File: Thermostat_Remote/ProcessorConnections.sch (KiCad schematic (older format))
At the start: 4 parts

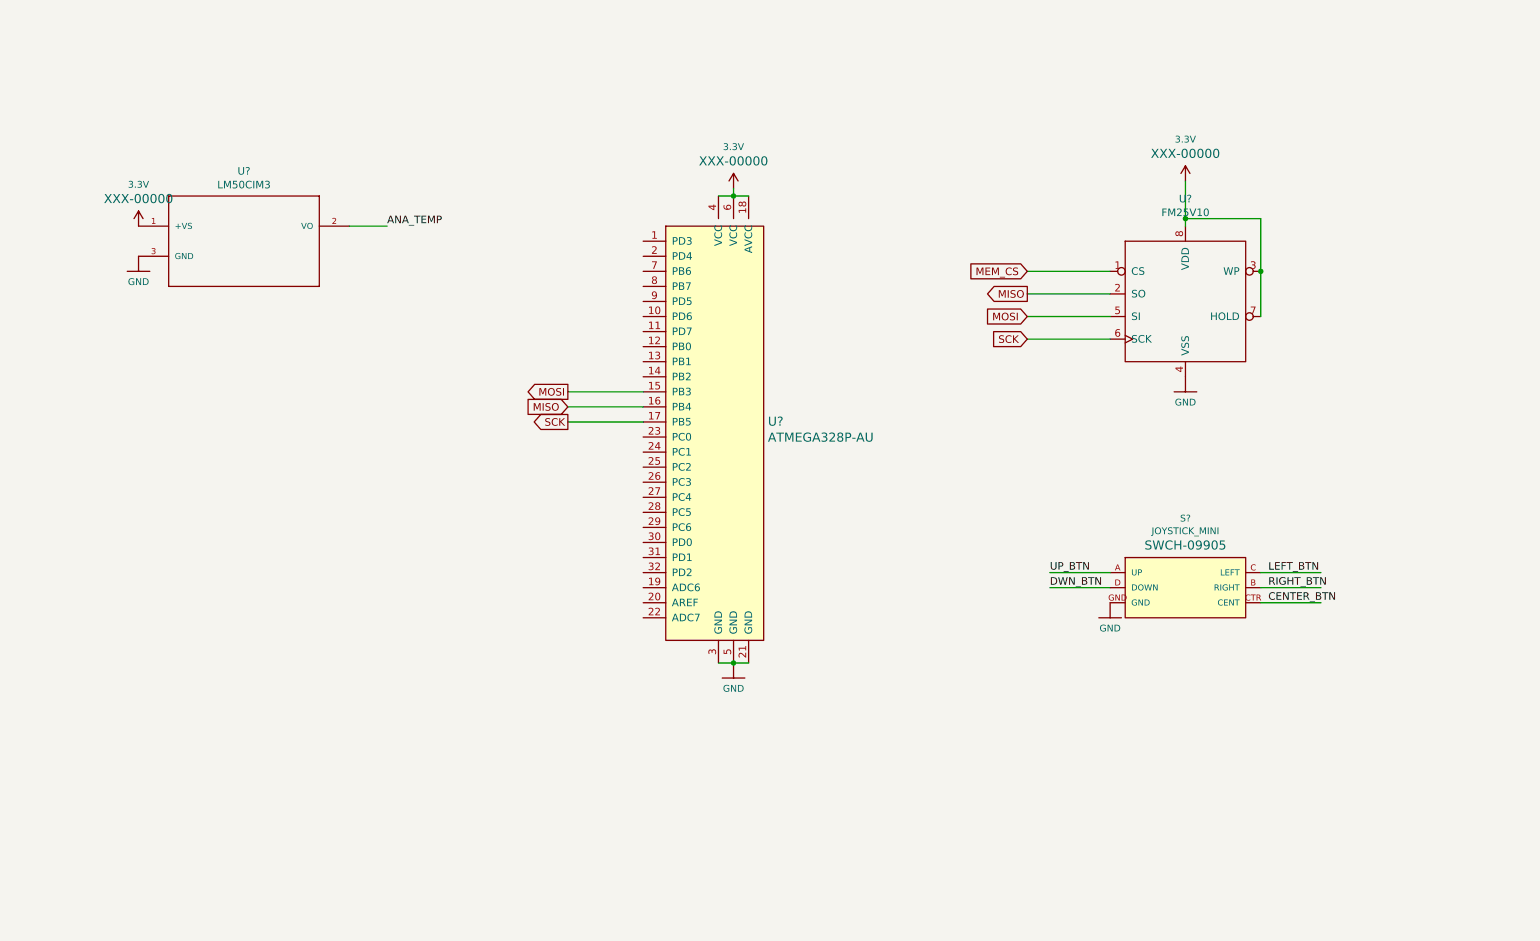
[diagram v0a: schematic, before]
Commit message: Update remote sensor layout
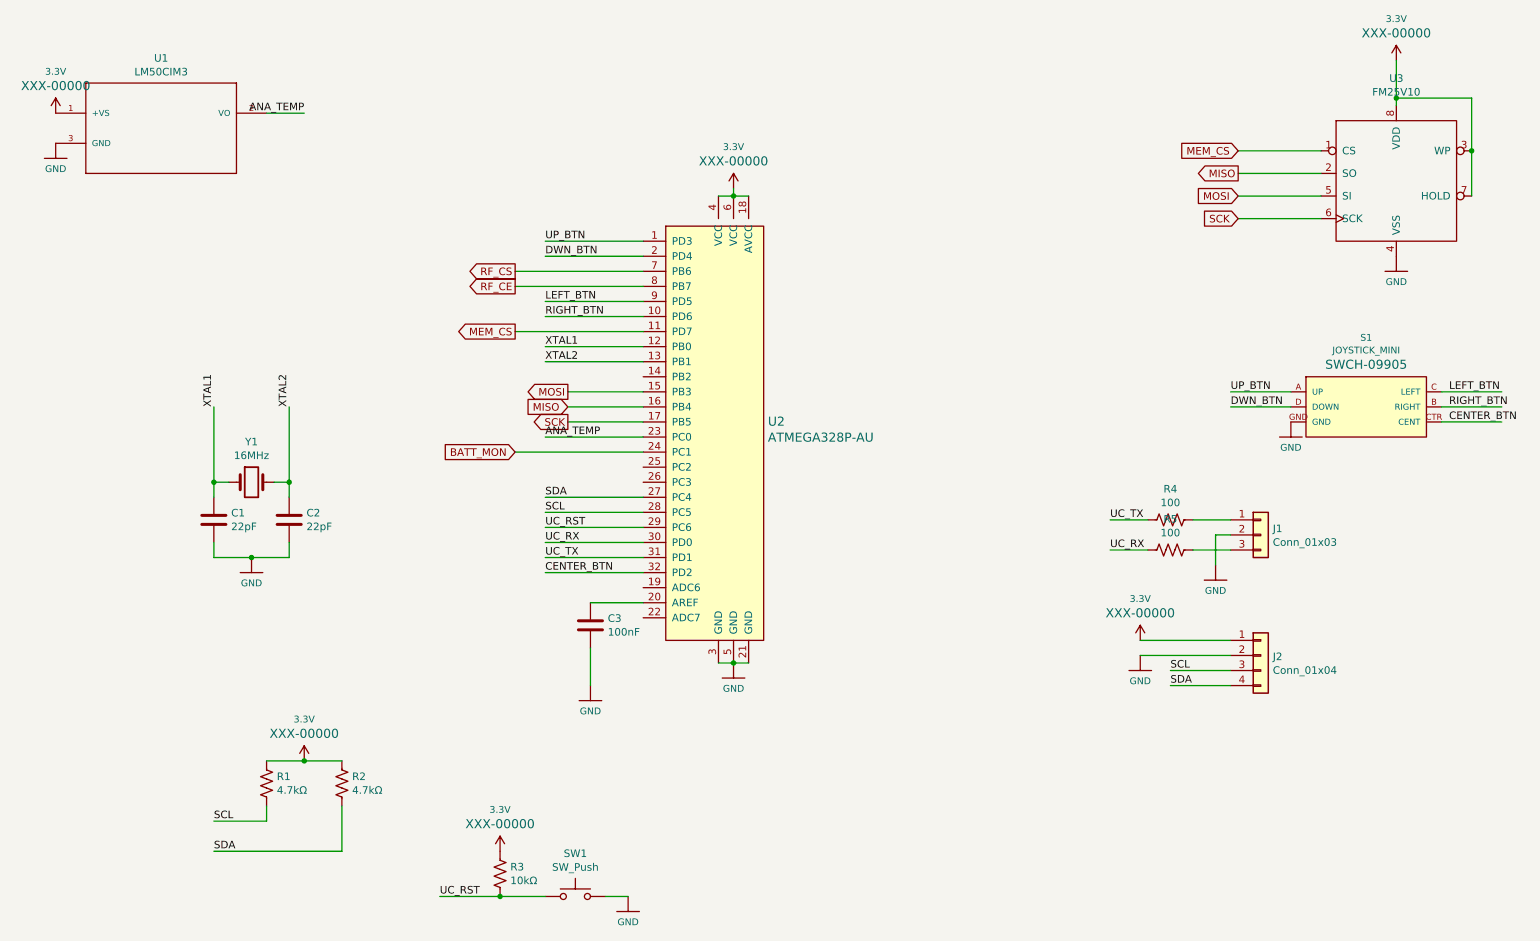
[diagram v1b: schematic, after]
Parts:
- added C1, C2: 22pF, Capacitor_SMD:C_0402_1005Metric, symbol Device:C
- added C3: 100nF, Capacitor_SMD:C_0402_1005Metric, symbol Device:C
- added J1: Conn_01x03, Connector_JST:JST_PH_S3B-PH-SM4-TB_1x03-1MP_P2.00mm_Horizontal, symbol Connector_Generic:Conn_01x03
- added J2: Conn_01x04, Connector_JST:JST_PH_B4B-PH-SM4-TB_1x04-1MP_P2.00mm_Vertical, symbol Connector_Generic:Conn_01x04
- added R1, R2: 4.7kΩ, Resistors:0402, symbol Device:R_US
- added R3: 10kΩ, Resistors:0402, symbol Device:R_US
- added R4, R5: 100, Resistors:0402, symbol Device:R_US
- added SW1: SW_Push, Button_Switch_SMD:SW_SPST_TL3342, symbol Switch:SW_Push
- added Y1: 16MHz, Crystal:Crystal_SMD_SeikoEpson_MC405-2Pin_9.6x4.1mm, symbol Device:Crystal
- gave numbers to parts that had none: 4
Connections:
- net labels added: BATT_MON, RF_CE, RF_CS, SCL, SDA, UC_RST, UC_RX, UC_TX, XTAL1, XTAL2
- wire segments 23 -> 71
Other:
- moved on the sheet: S1, U1, U3

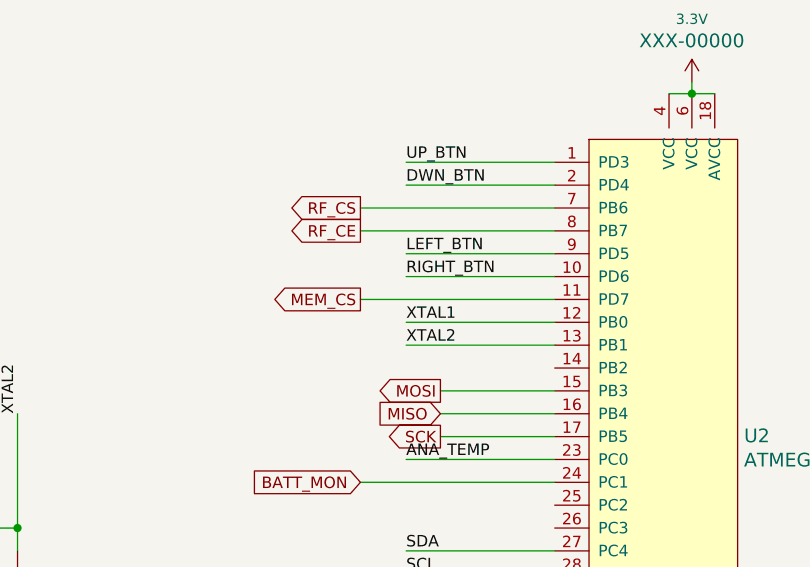
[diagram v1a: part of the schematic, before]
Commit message: Update processor pin definitions
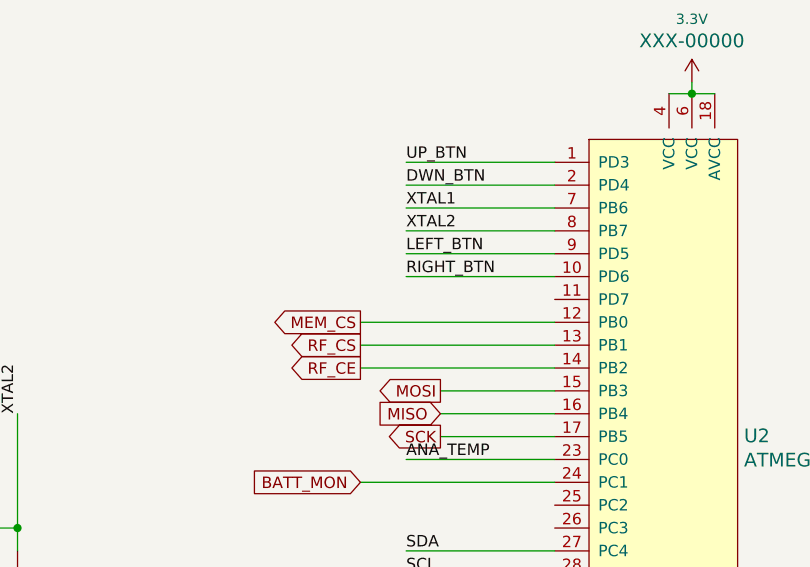
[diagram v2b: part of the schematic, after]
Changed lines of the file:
@@
 Text Label 4450 2550 0    50   ~ 0
 RIGHT_BTN
-Wire Wire Line
-	5100 2750 4450 2750
-Wire Wire Line
-	5100 2850 4450 2850
-Text Label 4450 2750 0    50   ~ 0
-XTAL1
-Text Label 4450 2850 0    50   ~ 0
-XTAL2
 $Comp
 L Device:Crystal Y1
@@
 Text Label 3750 6400 0    50   ~ 0
 UC_RST
-Wire Wire Line
-	5100 2250 4250 2250
-Wire Wire Line
-	5100 2350 4250 2350
-Wire Wire Line
-	5100 2650 4250 2650
-Text GLabel 4250 2650 0    50   Output ~ 0
-MEM_CS
-Text GLabel 4250 2350 0    50   Output ~ 0
-RF_CE
-Text GLabel 4250 2250 0    50   Output ~ 0
-RF_CS
 $Comp
 L SparkFun-PowerSymbols:3.3V #SUPPLY0105
@@
 Text GLabel 4250 3450 0    50   Input ~ 0
 BATT_MON
+Wire Wire Line
+	5100 2250 4450 2250
+Wire Wire Line
+	5100 2350 4450 2350
+Text Label 4450 2250 0    50   ~ 0
+XTAL1
+Text Label 4450 2350 0    50   ~ 0
+XTAL2
+Wire Wire Line
+	5100 2750 4250 2750
+Wire Wire Line
+	5100 2850 4250 2850
+Wire Wire Line
+	5100 2950 4250 2950
+Text GLabel 4250 2750 0    50   Output ~ 0
+MEM_CS
+Text GLabel 4250 2850 0    50   Output ~ 0
+RF_CS
+Text GLabel 4250 2950 0    50   Output ~ 0
+RF_CE
 $EndSCHEMATC
